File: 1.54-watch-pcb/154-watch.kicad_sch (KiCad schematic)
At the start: 66 parts, among them J1 AFC24-S24FIC-00, J2 Conn_01x06_Female, J3 USB_C_Programming, J4 Jack-DC, J5 Conn_01x02_Male, Q1 Si1308, Q2 BC817, Q3 BC817, Q4 Si2301CDS, SW1 RESET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

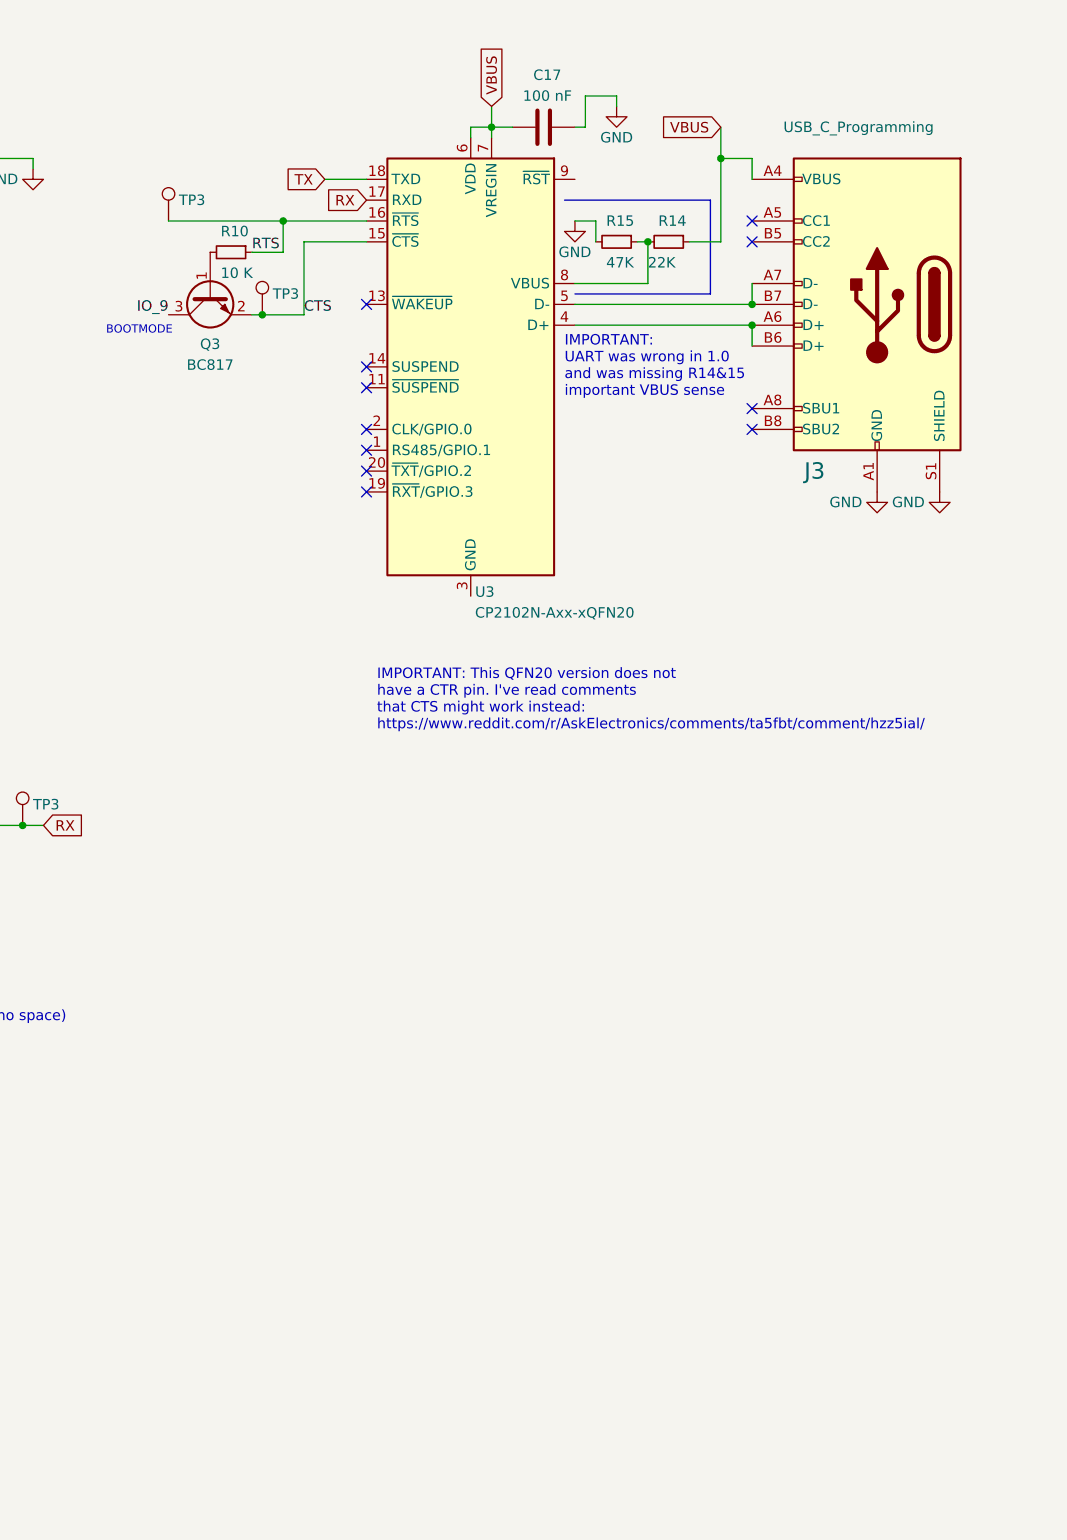
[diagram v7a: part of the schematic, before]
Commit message: Update UART in 1.54" watch PCB
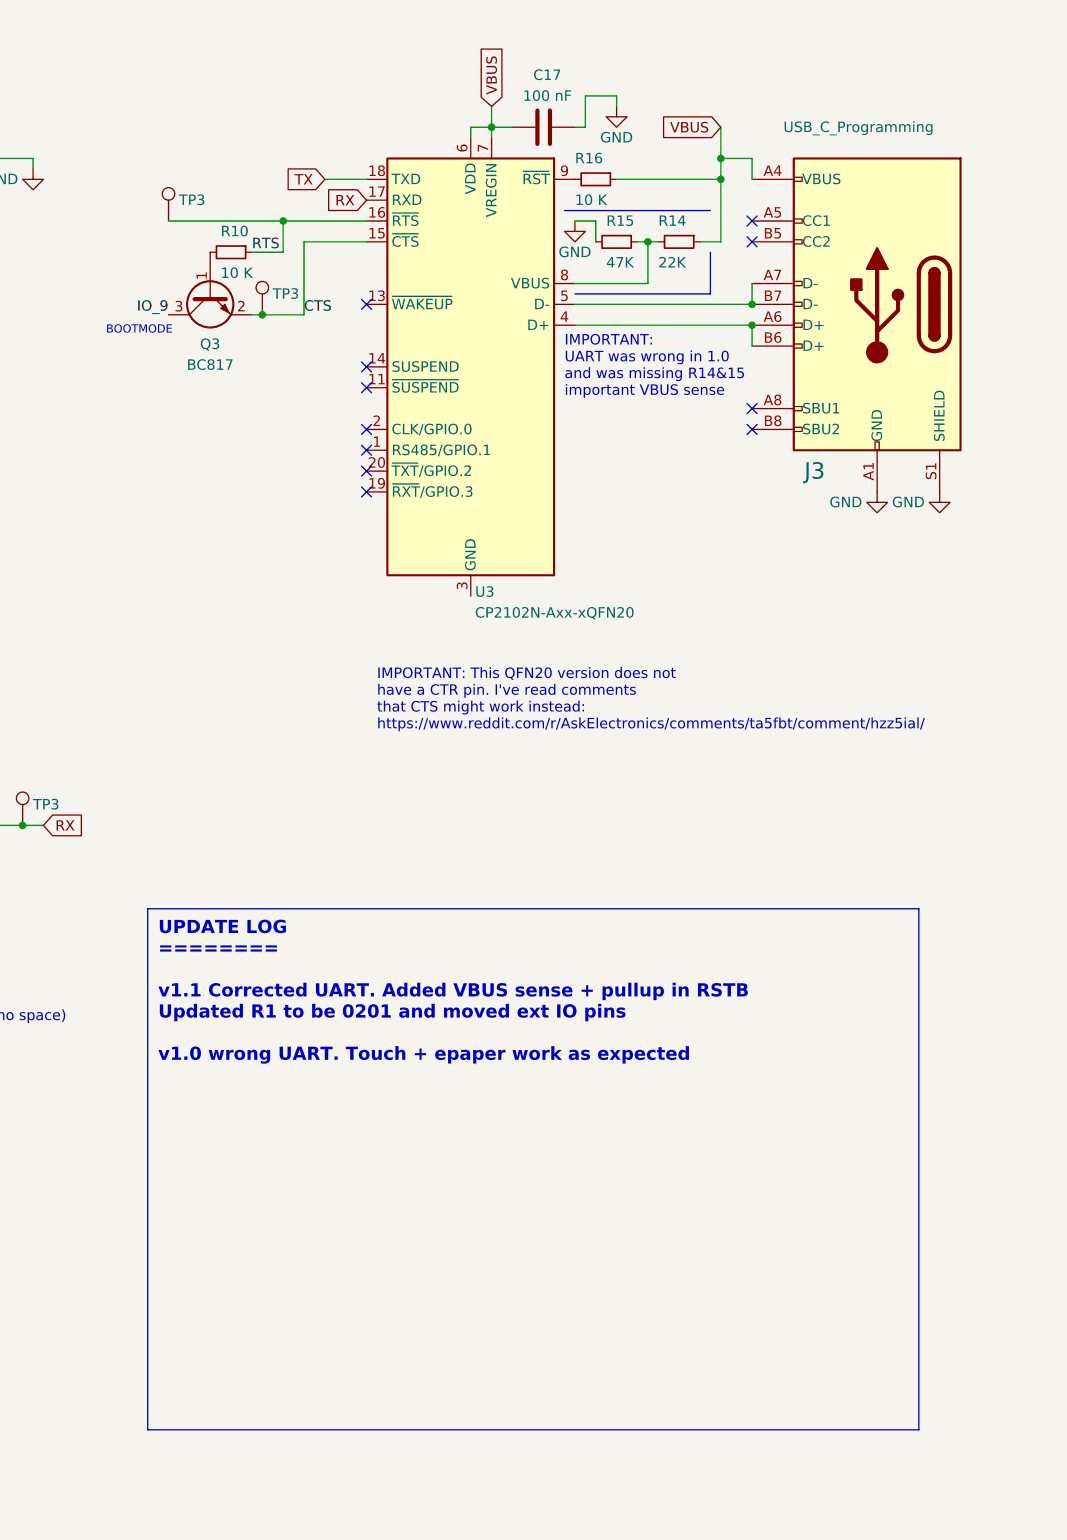
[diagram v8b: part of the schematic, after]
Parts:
- added R16: 10 K, Resistor_SMD:R_0402_1005Metric, symbol Device:R_Small
- R1: footprint Resistor_SMD:R_0603_1608Metric -> Resistor_SMD:R_0402_1005Metric; LCSC C25804 -> C319933
- R14: footprint Resistor_SMD:R_0603_1608Metric -> Resistor_SMD:R_0402_1005Metric; LCSC C31850 -> C227336
- R15: footprint Resistor_SMD:R_0603_1608Metric -> Resistor_SMD:R_0402_1005Metric; LCSC C137715 -> C2838676
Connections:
- net VBUS: now also R16.1
- net at U3.9 (~{RST}): now also R16.2
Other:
- moved on the sheet: R14
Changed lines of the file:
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@@
   (title_block
     (title "Goodisplay 24 pin adapter with touch for small epaper")
-    (rev "1.0")
+    (rev "1.1")
     (company "FASANI CORPORATION")
   )
@@
   (junction (at 287.02 143.51) (diameter 0) (color 0 0 0 0)
   )
+  (junction (at 372.11 64.77) (diameter 0) (color 0 0 0 0)
+  )
   (junction (at 281.94 128.27) (diameter 0) (color 0 0 0 0)
   )
@@
     (stroke (width 0) (type default))
   )
-  (wire (pts (xy 372.11 72.39) (xy 372.11 62.23))
+  (wire (pts (xy 372.11 72.39) (xy 372.11 64.77))
     (stroke (width 0) (type default))
   )
@@
     (stroke (width 0) (type default))
   )
-  (wire (pts (xy 368.3 72.39) (xy 372.11 72.39))
+  (wire (pts (xy 369.57 72.39) (xy 372.11 72.39))
     (stroke (width 0) (type default))
   )
@@
   )
   (polyline (pts (xy 354.33 78.74) (xy 370.84 78.74))
-    (stroke (width 0) (type default))
+    (stroke (width 0) (type default) (color 255 255 0 1))
   )
   (wire (pts (xy 323.85 64.77) (xy 328.93 64.77))
@@
     (stroke (width 0) (type default))
   )
+  (polyline (pts (xy 370.84 78.74) (xy 370.84 73.66))
+    (stroke (width 0) (type default) (color 255 255 0 1))
+  )
   (wire (pts (xy 213.36 71.12) (xy 220.98 71.12))
     (stroke (width 0) (type default))
@@
     (stroke (width 0) (type default))
   )
+  (wire (pts (xy 372.11 64.77) (xy 372.11 62.23))
+    (stroke (width 0) (type default))
+  )
   (wire (pts (xy 67.31 167.64) (xy 83.82 167.64))
     (stroke (width 0) (type default))
@@
     (stroke (width 0) (type default))
   )
-  (polyline (pts (xy 41.91 153.67) (xy 125.73 153.67))
+  (wire (pts (xy 364.49 72.39) (xy 363.22 72.39))
     (stroke (width 0) (type default))
   )
-  (polyline (pts (xy 370.84 67.31) (xy 370.84 78.74))
+  (polyline (pts (xy 41.91 153.67) (xy 125.73 153.67))
     (stroke (width 0) (type default))
   )
@@
     (stroke (width 0) (type default))
   )
+  (wire (pts (xy 359.41 64.77) (xy 372.11 64.77))
+    (stroke (width 0) (type default))
+  )
   (wire (pts (xy 92.71 167.64) (xy 92.71 163.83))
     (stroke (width 0) (type default))
@@
     (stroke (width 0) (type default))
   )
-  (polyline (pts (xy 353.06 67.31) (xy 370.84 67.31))
-    (stroke (width 0) (type default))
+  (polyline (pts (xy 353.06 68.58) (xy 370.84 68.58))
+    (stroke (width 0) (type default) (color 255 255 0 1))
   )
   (polyline (pts (xy 41.91 208.28) (xy 41.91 228.6))
@@
     (stroke (width 0) (type default))
   )
+  (text_box "UPDATE LOG\n========\n\nv1.1 Corrected UART. Added VBUS sense + pullup in RSTB\n      Updated R1 to be 0201 and moved ext IO pins\n\nv1.0 wrong UART. Touch + epaper work as expected"
+    (at 302.26 153.67 0) (size 93.98 63.5)
+    (stroke (width 0) (type default) (color 72 72 72 1))
+    (fill (type none))
+    (effects (font (size 1.6 1.6) (thickness 0.254) bold (color 72 72 72 1)) (justify left top))
+  )
   (text "PREVGL" (at 58.42 114.3 0)
     (effects (font (size 1.27 1.27)) (justify left bottom))
@@
       (effects (font (size 1.27 1.27)))
     )
-    (property "Footprint" "Resistor_SMD:R_0603_1608Metric" (at 69.85 62.738 90)
+    (property "Footprint" "Resistor_SMD:R_0402_1005Metric" (at 69.85 62.738 90)
       (effects (font (size 1.27 1.27)) hide)
     )
-    (property "Datasheet" "https://jlcpcb.com/partdetail/26547-0603WAF1002T5E/C25804" (at 69.85 60.96 0)
+    (property "Datasheet" "https://jlcpcb.com/partdetail/VikingTech-AR02DTD1002/C319933" (at 69.85 60.96 0)
       (effects (font (size 1.27 1.27)) hide)
     )
-    (property "LCSC" "C25804" (at 69.85 60.96 90)
+    (property "LCSC" "C319933" (at 69.85 60.96 90)
       (effects (font (size 1.27 1.27)) hide)
     )
@@
       (effects (font (size 1.27 1.27)) (justify left))
     )
-    (property "Footprint" "Resistor_SMD:R_0603_1608Metric" (at 359.41 72.39 0)
+    (property "Footprint" "Resistor_SMD:R_0402_1005Metric" (at 359.41 72.39 0)
       (effects (font (size 1.27 1.27)) hide)
     )
@@
       (effects (font (size 1.27 1.27)) hide)
     )
-    (property "LCSC" "C137715" (at 359.41 72.39 90)
+    (property "LCSC" "C2838676" (at 359.41 72.39 90)
       (effects (font (size 1.27 1.27)) hide)
     )
@@
     )
   )
+  (symbol (lib_id "Device:R_Small") (at 356.87 64.77 270) (unit 1)
+    (in_bom yes) (on_board yes) (dnp no)
+    (property "Reference" "R16" (at 354.33 62.23 90)
+      (effects (font (size 1.27 1.27)) (justify left))
+    )
+    (property "Value" "10 K" (at 354.33 67.31 90)
+      (effects (font (size 1.27 1.27)) (justify left))
+    )
+    (property "Footprint" "Resistor_SMD:R_0402_1005Metric" (at 356.87 64.77 0)
+      (effects (font (size 1.27 1.27)) hide)
+    )
+    (property "Datasheet" "https://jlcpcb.com/partdetail/VikingTech-AR02DTD1002/C319933" (at 356.87 64.77 0)
+      (effects (font (size 1.27 1.27)) hide)
+    )
+    (property "LCSC" "C319933" (at 356.87 64.77 90)
+      (effects (font (size 1.27 1.27)) hide)
+    )
+    (pin "1")
+    (pin "2")
+    (instances
+      (project "154-watch"
+        (path "/ea6fde00-59dc-4a79-a647-7e38199fae0e"
+          (reference "R16") (unit 1)
+        )
+      )
+    )
+  )
   (symbol (lib_id "power:GND") (at 172.72 82.55 0) (unit 1)
     (in_bom yes) (on_board yes) (dnp no) (fields_autoplaced)
@@
     )
   )
-  (symbol (lib_id "Device:R_Small") (at 365.76 72.39 270) (unit 1)
+  (symbol (lib_id "Device:R_Small") (at 367.03 72.39 270) (unit 1)
     (in_bom yes) (on_board yes) (dnp no)
     (property "Reference" "R14" (at 364.49 69.85 90)
       (effects (font (size 1.27 1.27)) (justify left))
     )
-    (property "Value" "22K" (at 363.22 74.93 90)
+    (property "Value" "22K" (at 364.49 74.93 90)
       (effects (font (size 1.27 1.27)) (justify left))
     )
-    (property "Footprint" "Resistor_SMD:R_0603_1608Metric" (at 365.76 72.39 0)
+    (property "Footprint" "Resistor_SMD:R_0402_1005Metric" (at 367.03 72.39 0)
       (effects (font (size 1.27 1.27)) hide)
     )
-    (property "Datasheet" "https://jlcpcb.com/partdetail/32812-0603WAF2202T5E/C31850" (at 365.76 72.39 0)
+    (property "Datasheet" "https://jlcpcb.com/partdetail/32812-0603WAF2202T5E/C31850" (at 367.03 72.39 0)
       (effects (font (size 1.27 1.27)) hide)
     )
-    (property "LCSC" "C31850" (at 365.76 72.39 90)
+    (property "LCSC" "C227336" (at 367.03 72.39 90)
       (effects (font (size 1.27 1.27)) hide)
     )
